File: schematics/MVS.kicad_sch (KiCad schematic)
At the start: 0 parts

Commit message: WIP
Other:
- added sheet NEO-E0  (neo-e0-stuff.kicad_sch)
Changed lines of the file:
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@@
     (comment 4 "NEO-GEO MVS MV1F")
   )
-  (sheet (at 24.13 101.6) (size 39.37 12.7) (fields_autoplaced)
+  (sheet (at 25.4 74.93) (size 38.1 12.7) (fields_autoplaced)
     (stroke (width 0.1524) (type solid))
     (fill (color 0 0 0 0.0000))
-    (property "Sheetname" "RGB DAC " (at 24.13 100.8884 0)
+    (property "Sheetname" "RGB DAC " (at 25.4 74.2184 0)
       (effects (font (size 1.27 1.27)) (justify left bottom))
     )
-    (property "Sheetfile" "RGBDAC.kicad_sch" (at 24.13 114.8846 0)
+    (property "Sheetfile" "RGBDAC.kicad_sch" (at 25.4 88.2146 0)
       (effects (font (size 1.27 1.27)) (justify left top))
     )
@@
     )
   )
-  (sheet (at 25.4 25.4) (size 38.1 12.7)
+  (sheet (at 25.4 17.78) (size 38.1 12.7)
     (stroke (width 0.1524) (type solid))
     (fill (color 0 0 0 0.0000))
-    (property "Sheetname" "68K BIOS - Working & Backup RAM" (at 25.4 24.6884 0)
+    (property "Sheetname" "68K BIOS - Working & Backup RAM" (at 25.4 17.0684 0)
       (effects (font (size 1.27 1.27)) (justify left bottom))
     )
-    (property "Sheetfile" "68KWBRAM.kicad_sch" (at 25.4 38.6846 0)
+    (property "Sheetfile" "68KWBRAM.kicad_sch" (at 25.4 31.0646 0)
       (effects (font (size 1.27 1.27)) (justify left top))
     )
-    (property "WIP" "DONE" (at 44.45 31.75 0)
+    (property "WIP" "DONE" (at 44.45 24.13 0)
       (effects (font (size 1.27 1.27)))
     )
@@
     )
   )
-  (sheet (at 25.4 76.2) (size 38.1 12.7) (fields_autoplaced)
+  (sheet (at 25.4 55.88) (size 38.1 12.7) (fields_autoplaced)
     (stroke (width 0.1524) (type solid))
     (fill (color 0 0 0 0.0000))
-    (property "Sheetname" "Clock" (at 25.4 75.4884 0)
+    (property "Sheetname" "Clock" (at 25.4 55.1684 0)
       (effects (font (size 1.27 1.27)) (justify left bottom))
     )
-    (property "Sheetfile" "clock.kicad_sch" (at 25.4 89.4846 0)
+    (property "Sheetfile" "clock.kicad_sch" (at 25.4 69.1646 0)
       (effects (font (size 1.27 1.27)) (justify left top))
     )
@@
     )
   )
-  (sheet (at 25.4 50.8) (size 38.1 12.7) (fields_autoplaced)
+  (sheet (at 25.4 36.83) (size 38.1 12.7) (fields_autoplaced)
     (stroke (width 0.1524) (type solid))
     (fill (color 0 0 0 0.0000))
-    (property "Sheetname" "Players Input " (at 25.4 50.0884 0)
+    (property "Sheetname" "Players Input " (at 25.4 36.1184 0)
       (effects (font (size 1.27 1.27)) (justify left bottom))
     )
-    (property "Sheetfile" "PlayersInput.kicad_sch" (at 25.4 64.0846 0)
+    (property "Sheetfile" "PlayersInput.kicad_sch" (at 25.4 50.1146 0)
       (effects (font (size 1.27 1.27)) (justify left top))
     )
@@
     )
   )
-  (sheet (at 76.2 76.2) (size 39.37 12.7) (fields_autoplaced)
+  (sheet (at 68.58 55.88) (size 38.1 12.7) (fields_autoplaced)
     (stroke (width 0.1524) (type solid))
     (fill (color 0 0 0 0.0000))
-    (property "Sheetname" "Battery & Saved Memory" (at 76.2 75.4884 0)
+    (property "Sheetname" "Battery & Saved Memory" (at 68.58 55.1684 0)
       (effects (font (size 1.27 1.27)) (justify left bottom))
     )
-    (property "Sheetfile" "BatterySaved.kicad_sch" (at 76.2 89.4846 0)
+    (property "Sheetfile" "BatterySaved.kicad_sch" (at 68.58 69.1646 0)
       (effects (font (size 1.27 1.27)) (justify left top))
     )
@@
       )
     )
+  )
+  (sheet (at 68.58 74.93) (size 38.1 12.7) (fields_autoplaced)
+    (stroke (width 0.1524) (type solid))
+    (fill (color 0 0 0 0.0000))
+    (property "Sheetname" "NEO-E0 " (at 68.58 74.2184 0)
+      (effects (font (size 1.27 1.27)) (justify left bottom))
+    )
+    (property "Sheetfile" "neo-e0-stuff.kicad_sch" (at 68.58 88.2146 0)
+      (effects (font (size 1.27 1.27)) (justify left top))
+    )
+    (instances
+      (project "MVS"
+        (path "/8d0803ab-15ed-47a7-8dcb-ab27dc5b29c2" (page "7"))
+      )
+    )

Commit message: WIP
starting Page 2 : LSPC2
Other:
- added sheet LSPC2-A2 & VRAM (lspc2-Vram.kicad_sch)
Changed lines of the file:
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@@
+    )
+  )
+  (sheet (at 68.58 17.78) (size 38.1 12.7) (fields_autoplaced)
+    (stroke (width 0.1524) (type solid))
+    (fill (color 0 0 0 0.0000))
+    (property "Sheetname" "LSPC2-A2 & VRAM" (at 68.58 17.0684 0)
+      (effects (font (size 1.27 1.27)) (justify left bottom))
+    )
+    (property "Sheetfile" "lspc2-Vram.kicad_sch" (at 68.58 31.0646 0)
+      (effects (font (size 1.27 1.27)) (justify left top))
+    )
+    (instances
+      (project "MVS"
+        (path "/8d0803ab-15ed-47a7-8dcb-ab27dc5b29c2" (page "8"))
+      )
     )
   )

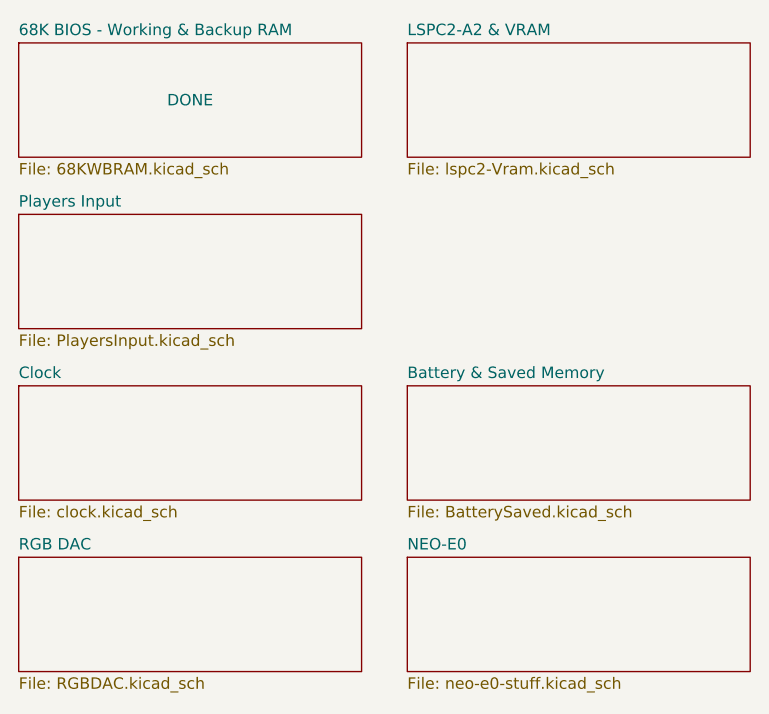
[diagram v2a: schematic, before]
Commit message: update "main" schematics
Adding LSPC2-A2, NEO-B1, L0 ROM
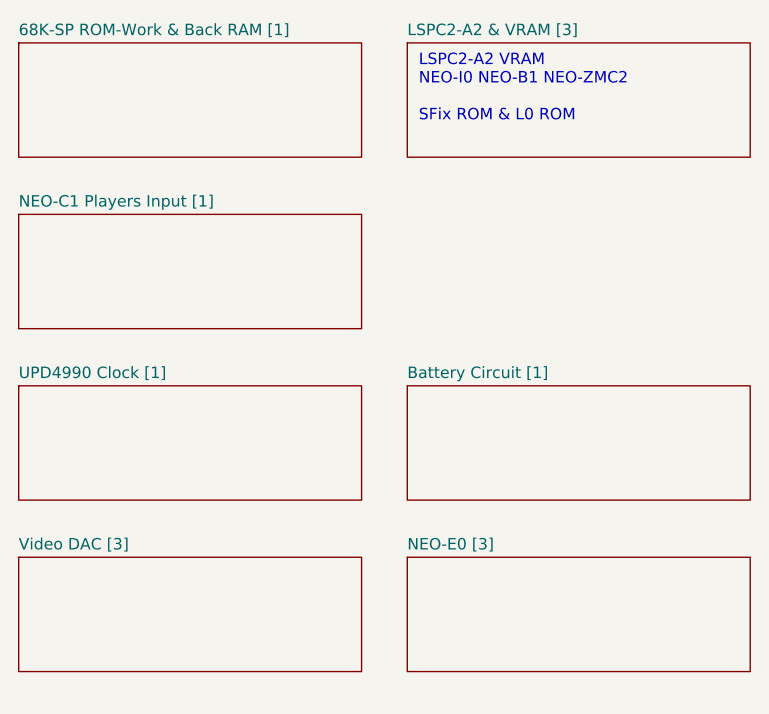
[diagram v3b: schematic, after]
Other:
- sheet 68K BIOS - Working & Backup RAM renamed 68K-SP ROM-Work & Back RAM [1]
- sheet Battery & Saved Memory renamed Battery Circuit [1]
- sheet Clock renamed UPD4990 Clock [1]
- sheet LSPC2-A2 & VRAM renamed LSPC2-A2 & VRAM [3]
- sheet NEO-E0  renamed NEO-E0 [3]
- sheet Players Input  renamed NEO-C1 Players Input [1]
- sheet RGB DAC  renamed Video DAC [3]
- note added: "LSPC2-A2 VRAM NEO-I0 NEO-B1 NEO-ZMC2 SFix ROM & L0 ROM"
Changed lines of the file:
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@@
     (comment 4 "NEO-GEO MVS MV1F")
+  )
+  (text "LSPC2-A2 VRAM \nNEO-I0 NEO-B1 NEO-ZMC2 \n\nSFix ROM & L0 ROM"
+    (at 69.85 26.67 0)
+    (effects (font (size 1.27 1.27)) (justify left bottom))
   )
   (sheet (at 25.4 74.93) (size 38.1 12.7) (fields_autoplaced)
     (stroke (width 0.1524) (type solid))
     (fill (color 0 0 0 0.0000))
-    (property "Sheetname" "RGB DAC " (at 25.4 74.2184 0)
+    (property "Sheetname" "Video DAC [3]" (at 25.4 74.2184 0)
       (effects (font (size 1.27 1.27)) (justify left bottom))
     )
     (property "Sheetfile" "RGBDAC.kicad_sch" (at 25.4 88.2146 0)
-      (effects (font (size 1.27 1.27)) (justify left top))
+      (effects (font (size 1.27 1.27)) (justify left top) hide)
     )
     (instances
@@
     (stroke (width 0.1524) (type solid))
     (fill (color 0 0 0 0.0000))
-    (property "Sheetname" "68K BIOS - Working & Backup RAM" (at 25.4 17.0684 0)
+    (property "Sheetname" "68K-SP ROM-Work & Back RAM [1]" (at 25.4 17.0684 0)
       (effects (font (size 1.27 1.27)) (justify left bottom))
     )
     (property "Sheetfile" "68KWBRAM.kicad_sch" (at 25.4 31.0646 0)
-      (effects (font (size 1.27 1.27)) (justify left top))
-    )
-    (property "WIP" "DONE" (at 44.45 24.13 0)
-      (effects (font (size 1.27 1.27)))
+      (effects (font (size 1.27 1.27)) (justify left top) hide)
     )
     (instances
@@
     (stroke (width 0.1524) (type solid))
     (fill (color 0 0 0 0.0000))
-    (property "Sheetname" "Clock" (at 25.4 55.1684 0)
+    (property "Sheetname" "UPD4990 Clock [1]" (at 25.4 55.1684 0)
       (effects (font (size 1.27 1.27)) (justify left bottom))
     )
     (property "Sheetfile" "clock.kicad_sch" (at 25.4 69.1646 0)
-      (effects (font (size 1.27 1.27)) (justify left top))
+      (effects (font (size 1.27 1.27)) (justify left top) hide)
     )
     (instances
@@
     (stroke (width 0.1524) (type solid))
     (fill (color 0 0 0 0.0000))
-    (property "Sheetname" "Players Input " (at 25.4 36.1184 0)
+    (property "Sheetname" "NEO-C1 Players Input [1]" (at 25.4 36.1184 0)
       (effects (font (size 1.27 1.27)) (justify left bottom))
     )
     (property "Sheetfile" "PlayersInput.kicad_sch" (at 25.4 50.1146 0)
-      (effects (font (size 1.27 1.27)) (justify left top))
+      (effects (font (size 1.27 1.27)) (justify left top) hide)
     )
     (instances
@@
     )
   )
-  (sheet (at 68.58 17.78) (size 38.1 12.7) (fields_autoplaced)
+  (sheet (at 68.58 17.78) (size 38.1 12.7)
     (stroke (width 0.1524) (type solid))
     (fill (color 0 0 0 0.0000))
-    (property "Sheetname" "LSPC2-A2 & VRAM" (at 68.58 17.0684 0)
+    (property "Sheetname" "LSPC2-A2 & VRAM [3]" (at 68.58 17.0684 0)
       (effects (font (size 1.27 1.27)) (justify left bottom))
     )
     (property "Sheetfile" "lspc2-Vram.kicad_sch" (at 68.58 31.0646 0)
-      (effects (font (size 1.27 1.27)) (justify left top))
+      (effects (font (size 1.27 1.27)) (justify left top) hide)
     )
     (instances
@@
     (stroke (width 0.1524) (type solid))
     (fill (color 0 0 0 0.0000))
-    (property "Sheetname" "Battery & Saved Memory" (at 68.58 55.1684 0)
+    (property "Sheetname" "Battery Circuit [1]" (at 68.58 55.1684 0)
       (effects (font (size 1.27 1.27)) (justify left bottom))
     )
     (property "Sheetfile" "BatterySaved.kicad_sch" (at 68.58 69.1646 0)
-      (effects (font (size 1.27 1.27)) (justify left top))
+      (effects (font (size 1.27 1.27)) (justify left top) hide)
     )
     (instances
@@
     (stroke (width 0.1524) (type solid))
     (fill (color 0 0 0 0.0000))
-    (property "Sheetname" "NEO-E0 " (at 68.58 74.2184 0)
+    (property "Sheetname" "NEO-E0 [3]" (at 68.58 74.2184 0)
       (effects (font (size 1.27 1.27)) (justify left bottom))
     )
     (property "Sheetfile" "neo-e0-stuff.kicad_sch" (at 68.58 88.2146 0)
-      (effects (font (size 1.27 1.27)) (justify left top))
+      (effects (font (size 1.27 1.27)) (justify left top) hide)
     )
     (instances

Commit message: Complete pages 1-4
completion of pages 1 to 4
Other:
- added sheet Audio [4] (Audio.kicad_sch)
- note added: "Z80, SM1 NEO-D0, YM2610 - YM3016D"
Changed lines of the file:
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@@
     (comment 4 "NEO-GEO MVS MV1F")
+  )
+  (text "Z80, SM1\nNEO-D0, YM2610 - YM3016D" (at 114.3 22.86 0)
+    (effects (font (size 1.27 1.27)) (justify left bottom))
   )
   (text "LSPC2-A2 VRAM \nNEO-I0 NEO-B1 NEO-ZMC2 \n\nSFix ROM & L0 ROM"
@@
       )
     )
+  )
+  (sheet (at 113.03 17.78) (size 38.1 12.7) (fields_autoplaced)
+    (stroke (width 0.1524) (type solid))
+    (fill (color 0 0 0 0.0000))
+    (property "Sheetname" "Audio [4]" (at 113.03 17.0684 0)
+      (effects (font (size 1.27 1.27)) (justify left bottom))
+    )
+    (property "Sheetfile" "Audio.kicad_sch" (at 113.03 31.0646 0)
+      (effects (font (size 1.27 1.27)) (justify left top) hide)
+    )
+    (instances
+      (project "MVS"
+        (path "/8d0803ab-15ed-47a7-8dcb-ab27dc5b29c2" (page "9"))
+      )
+    )

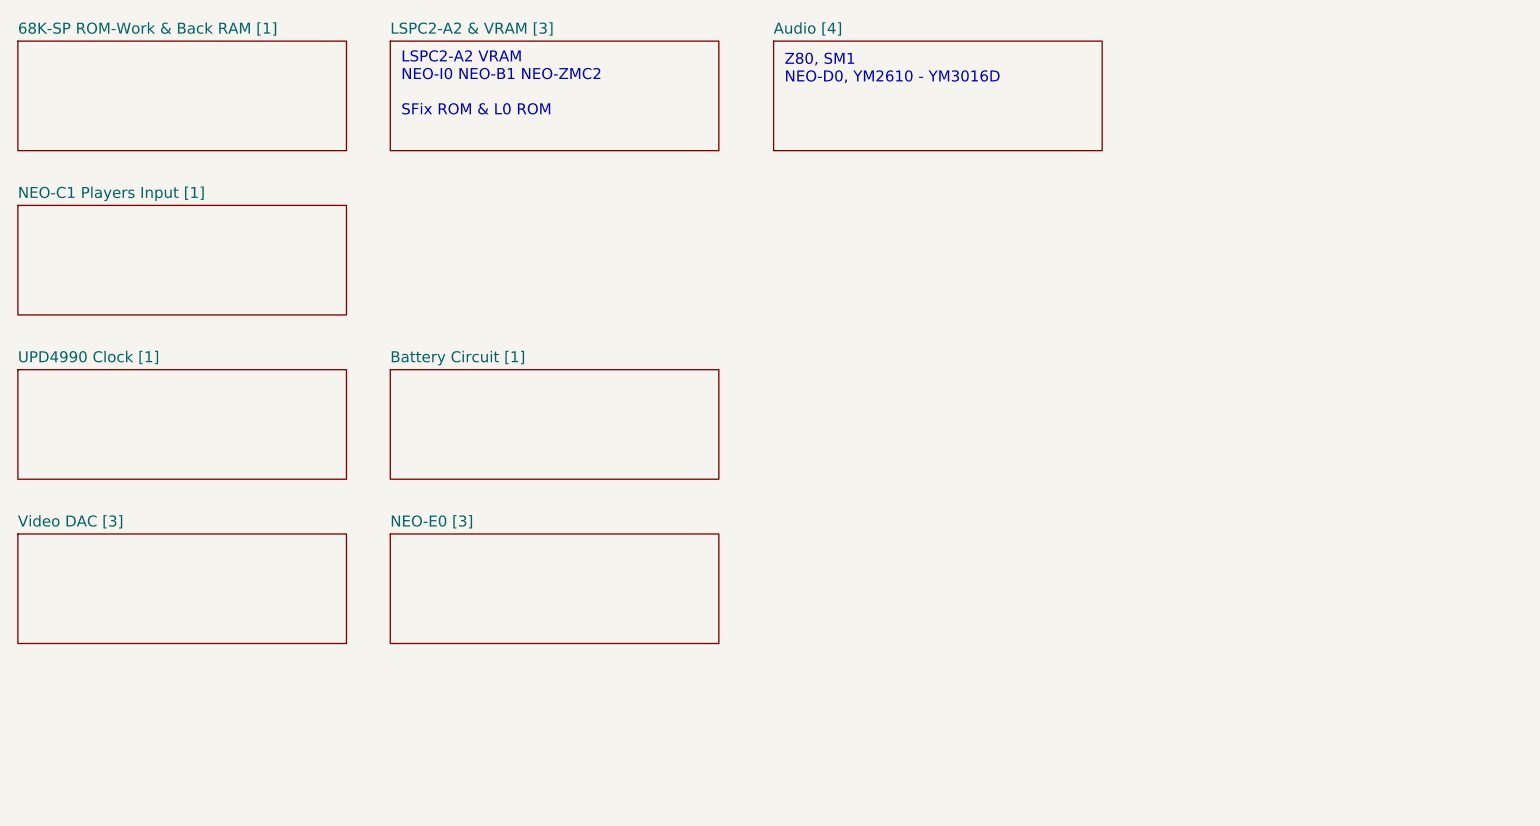
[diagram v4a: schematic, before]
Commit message: Audio Amp + player's button LED & marquee + Coins Up + 45% raiser card connectors
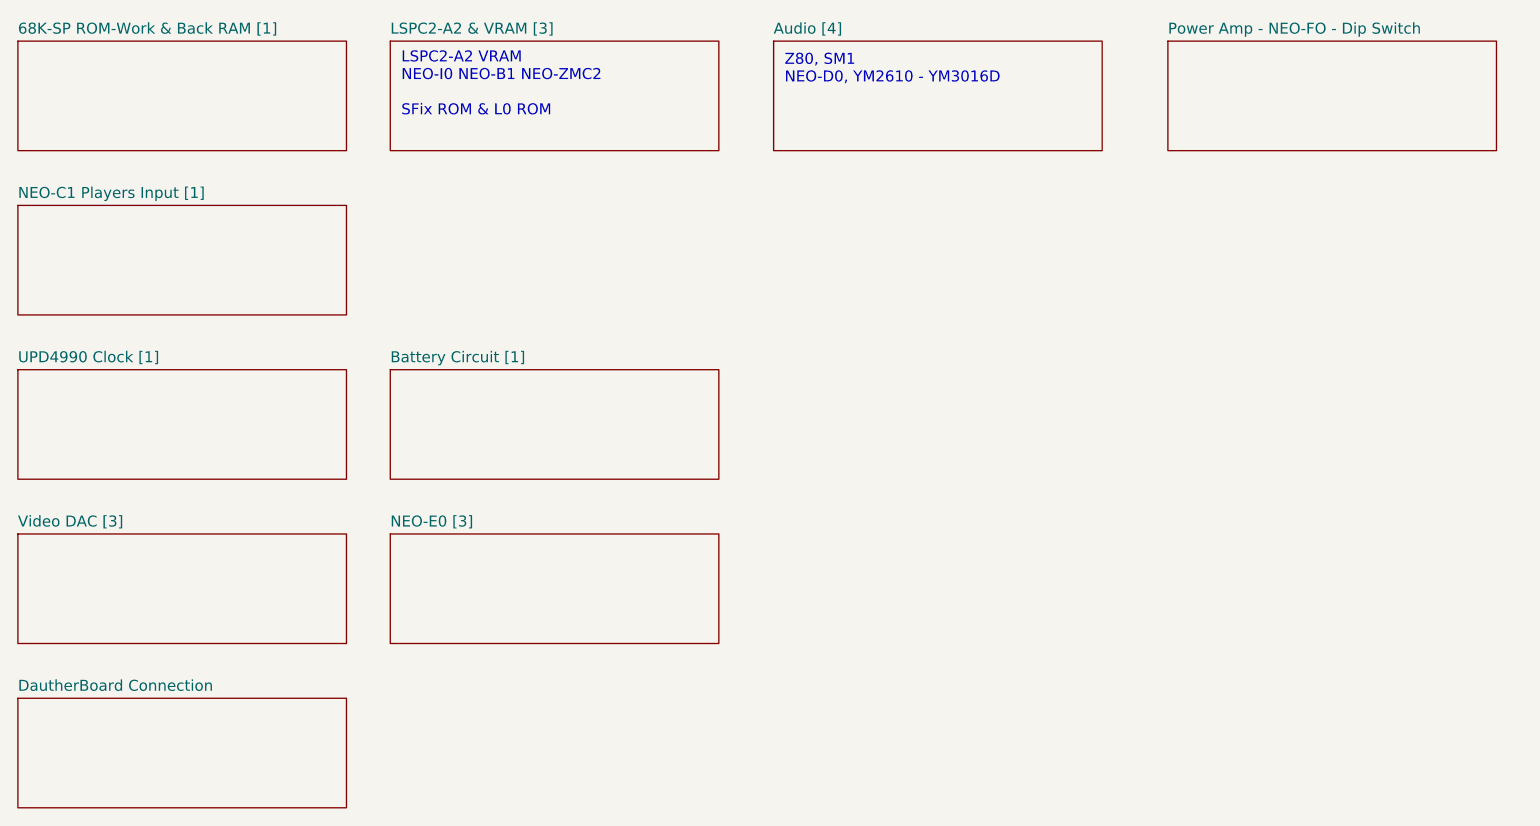
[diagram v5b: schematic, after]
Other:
- added sheet DautherBoard Connection (DaughterBoard.kicad_sch)
- added sheet Power Amp - NEO-FO - Dip Switch (PowerAmp-Neo-FO-Dip.kicad_sch)
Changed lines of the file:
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@@
+    )
+  )
+  (sheet (at 158.75 17.78) (size 38.1 12.7) (fields_autoplaced)
+    (stroke (width 0.1524) (type solid))
+    (fill (color 0 0 0 0.0000))
+    (property "Sheetname" "Power Amp - NEO-FO - Dip Switch" (at 158.75 17.0684 0)
+      (effects (font (size 1.27 1.27)) (justify left bottom))
+    )
+    (property "Sheetfile" "PowerAmp-Neo-FO-Dip.kicad_sch" (at 158.75 31.0646 0)
+      (effects (font (size 1.27 1.27)) (justify left top) hide)
+    )
+    (instances
+      (project "MVS"
+        (path "/8d0803ab-15ed-47a7-8dcb-ab27dc5b29c2" (page "10"))
+      )
     )
   )
@@
       )
     )
+  )
+  (sheet (at 25.4 93.98) (size 38.1 12.7) (fields_autoplaced)
+    (stroke (width 0.1524) (type solid))
+    (fill (color 0 0 0 0.0000))
+    (property "Sheetname" "DautherBoard Connection" (at 25.4 93.2684 0)
+      (effects (font (size 1.27 1.27)) (justify left bottom))
+    )
+    (property "Sheetfile" "DaughterBoard.kicad_sch" (at 25.4 107.2646 0)
+      (effects (font (size 1.27 1.27)) (justify left top) hide)
+    )
+    (instances
+      (project "MVS"
+        (path "/8d0803ab-15ed-47a7-8dcb-ab27dc5b29c2" (page "11"))
+      )
+    )

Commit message: typos
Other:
- title: (none) -> MVS MV1F
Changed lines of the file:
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@@
   (paper "A4")
   (title_block
+    (title "MVS MV1F")
     (date "2023-08-15")
     (rev "1.0")
@@
     (comment 3 "Converted by Frater ")
     (comment 4 "NEO-GEO MVS MV1F")
+    (comment 9 "https://github.com/Neo-Geo-Hardwares/Schematics-MV1F")
   )
   (text "Z80, SM1\nNEO-D0, YM2610 - YM3016D" (at 114.3 22.86 0)
